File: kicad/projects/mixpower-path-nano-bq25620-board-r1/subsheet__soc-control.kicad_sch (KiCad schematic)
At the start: 18 parts, among them Q7 Si1026X, U10 TJ-S1615CY6TGLCCYRGY-A5, U9 STM32G071G8U6N

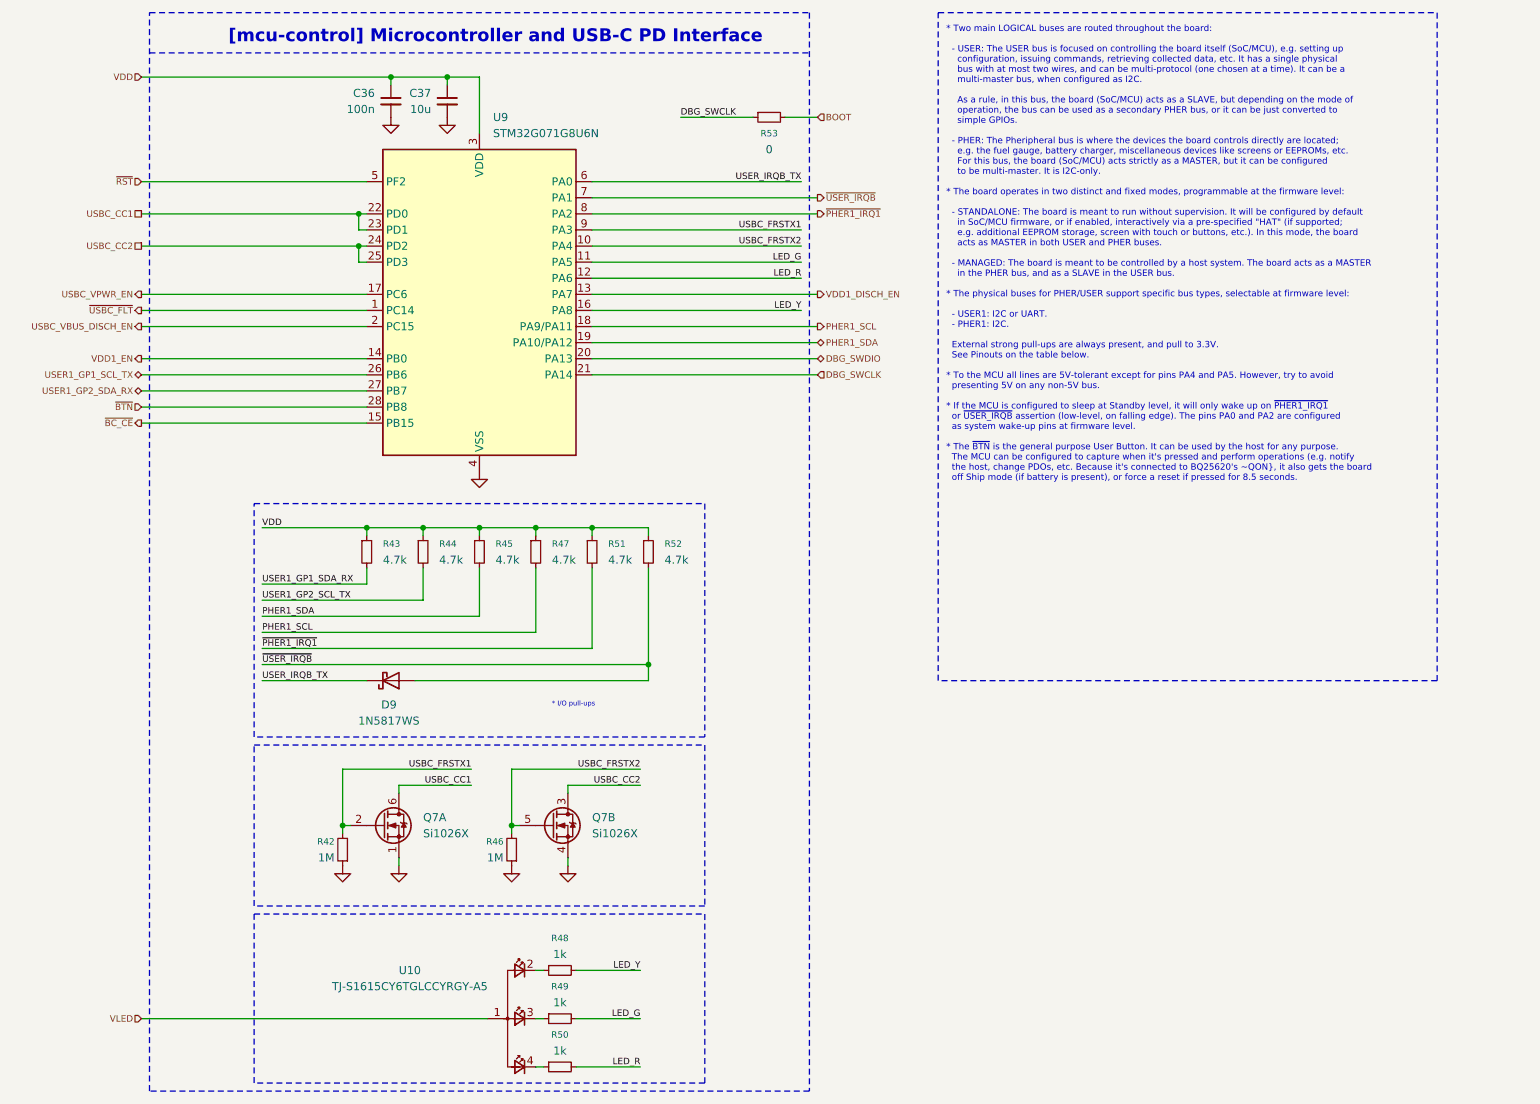
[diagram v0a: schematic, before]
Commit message: fix: put all subsheets in root of the Kicad project, regenerate schematics plots
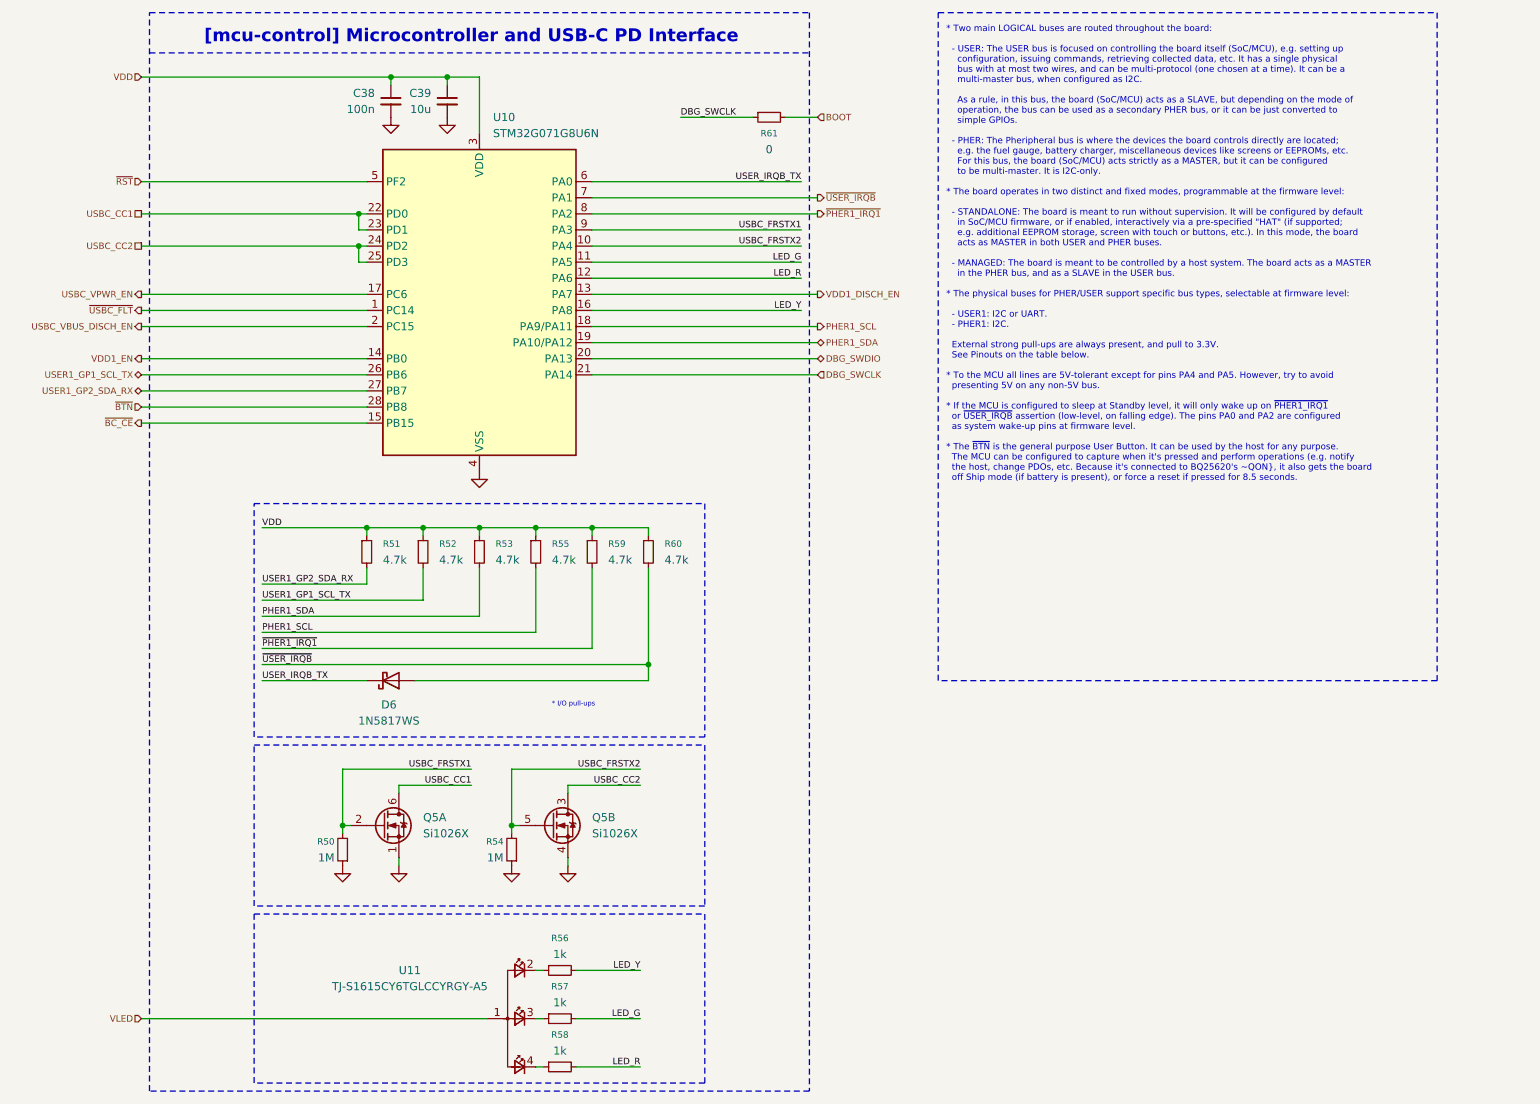
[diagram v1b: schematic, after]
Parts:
- renumbered C36 to C38, C37 to C39, D9 to D6, Q7 to Q5, R42 to R50, R43 to R51, R44 to R52, R45 to R53, R46 to R54, R47 to R55, R48 to R56, R49 to R57, R50 to R58, R51 to R59, R52 to R60, R53 to R61, U9 to U10, U10 to U11
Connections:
- net USER1_GP1_SDA_RX is gone; now on net USER1_GP2_SDA_RX: R51.2
- net USER1_GP2_SCL_TX is gone; now on net USER1_GP1_SCL_TX: R52.2
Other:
- title: (none) -> mixpower-path-nano-bq25620-board
